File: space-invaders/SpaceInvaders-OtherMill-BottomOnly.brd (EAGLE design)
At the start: 127 x 101.6 mm, 26 parts, among them J2_J4 TM4C123GXL, J3_J1 TM4C123GXL, J5 Nokia 5110, J6 Nokia 5110, U1 5V Voltage Regulator

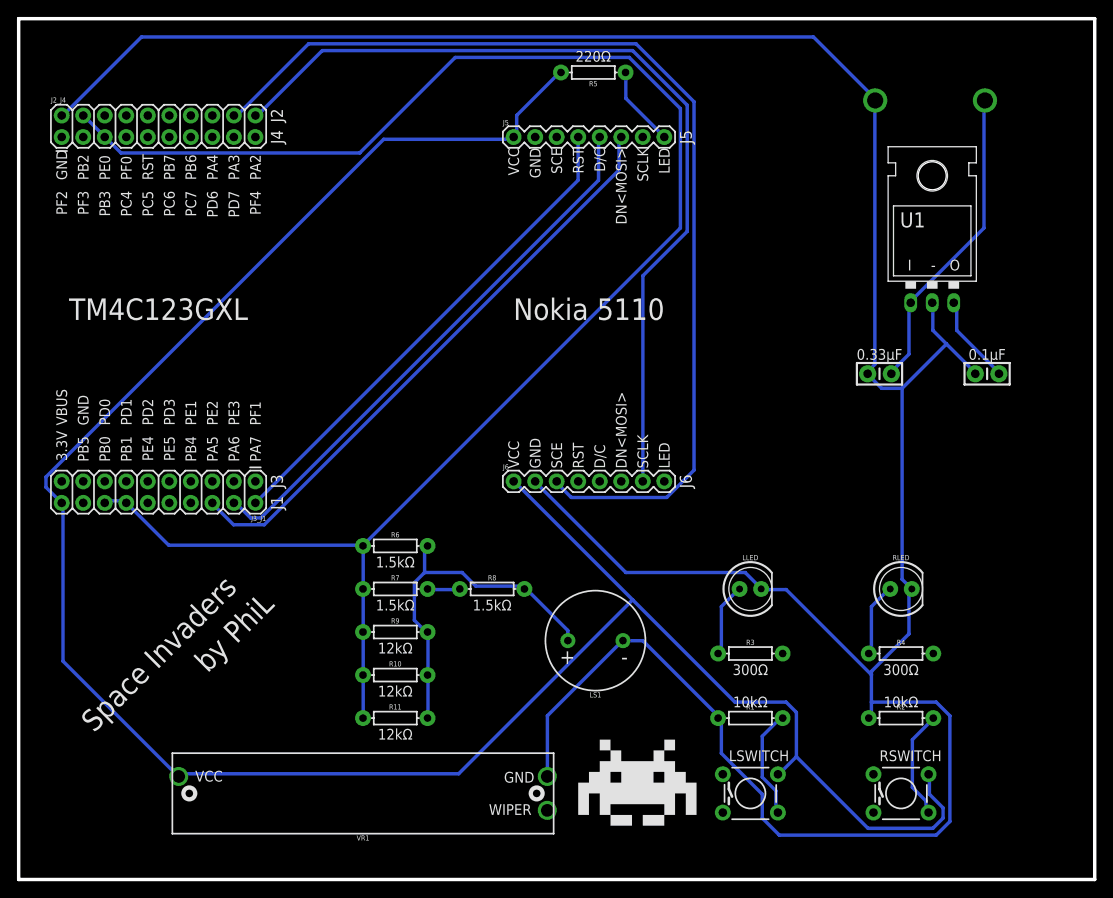
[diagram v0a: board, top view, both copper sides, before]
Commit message: Remove Top layer & Edit Bottom layer
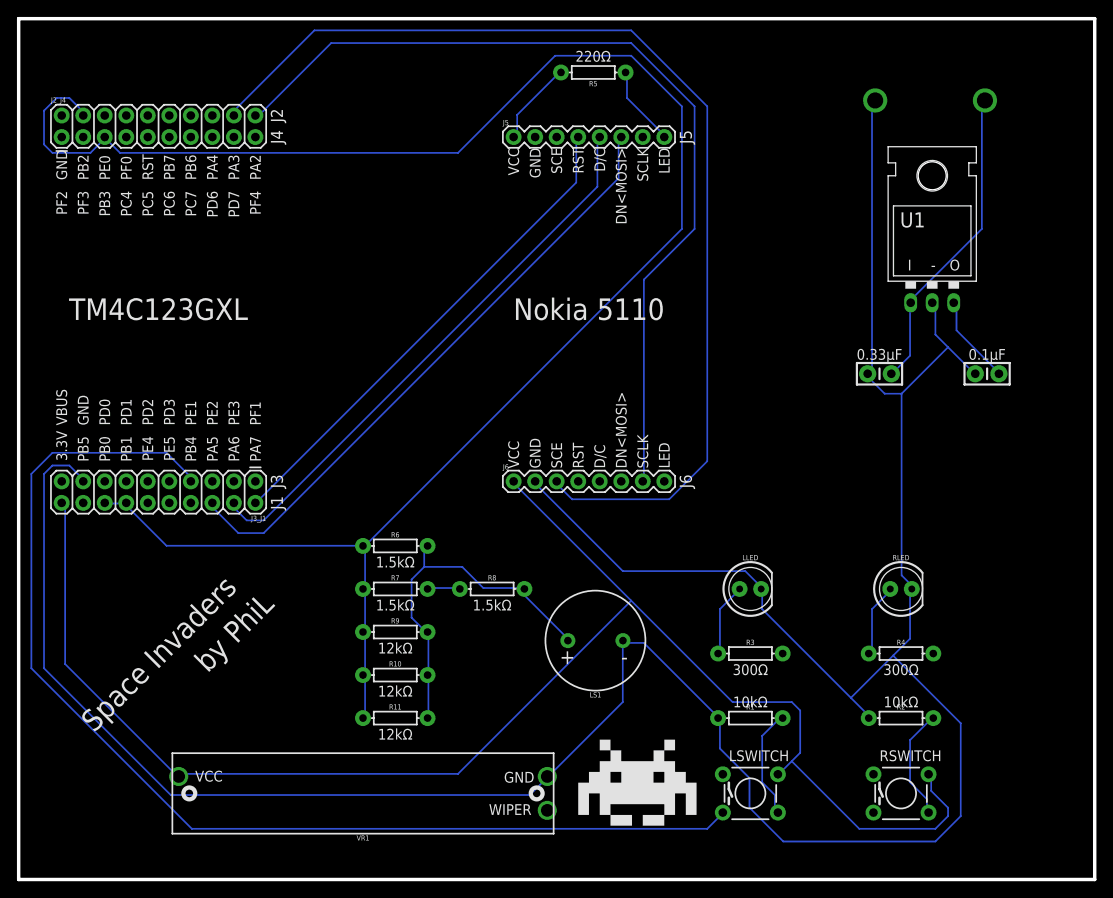
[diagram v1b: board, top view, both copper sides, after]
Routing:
- net PE1: track 0.00 -> 134.8 mm
- net 3.3V: track 266.3 -> 192.7 mm
- net PB2: track 199.9 -> 216.5 mm
- net PA3: track 122.5 -> 127.3 mm
- net GND: track 344.2 -> 341.1 mm
- net PA2: track 103.4 -> 105.2 mm
- net PA5: track 70.4 -> 72.0 mm
- net PA6: track 65.4 -> 66.3 mm
- net N$23: track 42.8 -> 43.4 mm
- removed copper zone on layer 1, net GND

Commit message: Reposition SpaceInvaders board layout
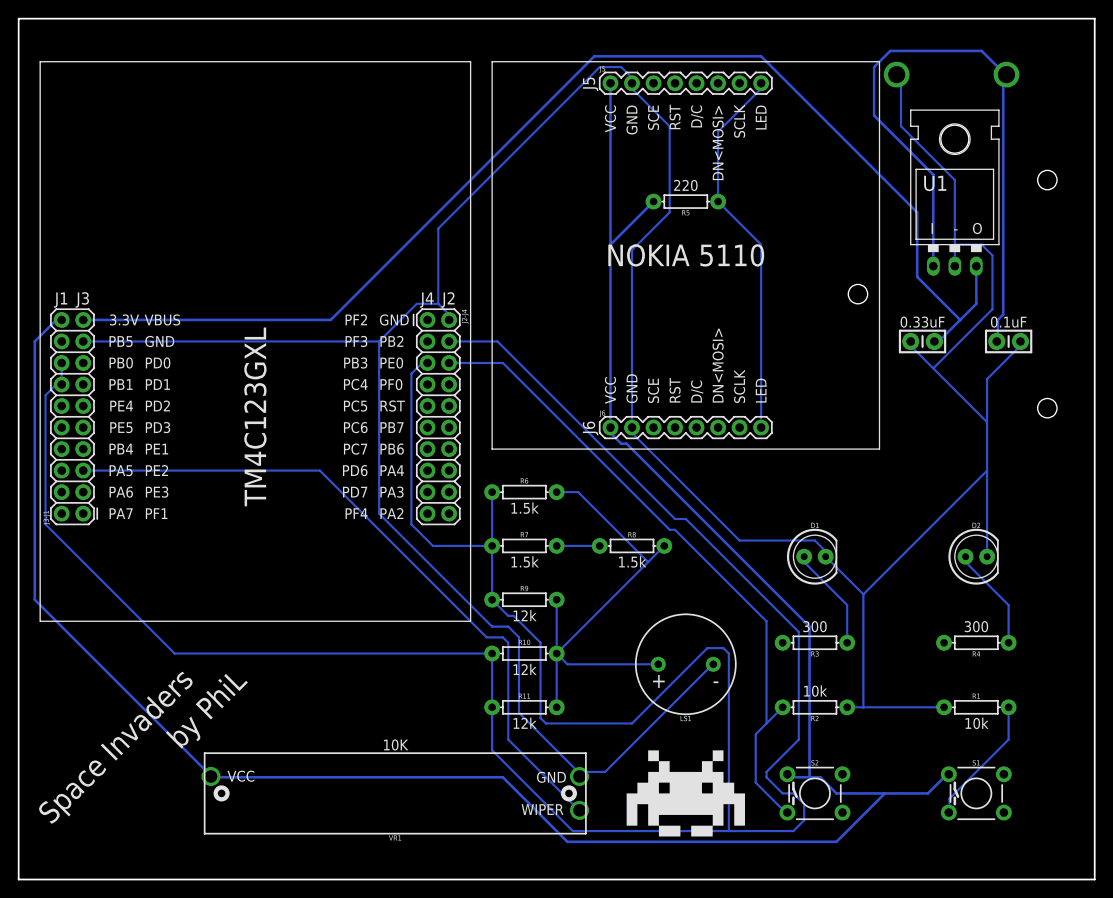
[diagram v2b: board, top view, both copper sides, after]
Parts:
- removed G1: 9V, SparkFun-Batteries:BATTCON_9V
- removed J2_J4, J3_J1: TM4C123GXL, SparkFun-Connectors:2X10
- removed LLED: YELLOW, SparkFun-LED:LED_5MM
- removed LSWITCH, RSWITCH: TACTILE, SparkFun-Retired:TACTILE-PTH
- removed RLED: RED, SparkFun-LED:LED_5MM
- added D1: YELLOW, SparkFun-LED:LED_5MM
- added D2: RED, SparkFun-LED:LED_5MM
- added J2-J4, J3-J1: TM4C123GXL, SparkFun-Connectors:2X10
- added J7: 9V, SparkFun-Connectors:BC9VPC
- added S1: SPECIAL, SparkFun-Switches:TACTILE_SWITCH_PTH_6.0MM
- added S2: REGULAR, SparkFun-Switches:TACTILE_SWITCH_PTH_6.0MM
- C1: value 0.1μF -> 0.1uF
- C2: value 0.33μF -> 0.33uF
- J5, J6: value Nokia 5110 -> Nokia_5110
- LS1: value BUZZER-PTH -> BUZZER
- R1, R2, VR1: value 10kΩ -> 10k
- R10, R11, R9: value 12kΩ -> 12k
- R3, R4: value 300Ω -> 300
- R5: value 220Ω -> 220
- R6, R7, R8: value 1.5kΩ -> 1.5k
- U1: value 5V Voltage Regulator -> LM7805CT
- moved R1 26.7 mm to (113.0, 20.3)
- moved R5 18.7 mm to (78.7, 80.0)
- moved R8 17.3 mm to (72.4, 39.4)
- moved R6 16.5 mm to (59.7, 45.7)
- moved R7 16.1 mm to (59.7, 39.4)
- moved C2 15.7 mm to (116.8, 63.5), turned to 0 degrees
- moved R9 15.7 mm to (59.7, 33.0)
- moved R10 15.5 mm to (59.7, 26.7)
- moved R11 15.3 mm to (59.7, 20.3)
- moved J5 13.1 mm to (69.8, 94.0)
- moved J6 13.1 mm to (69.8, 53.3)
- moved LS1 11.0 mm to (78.7, 25.4)
- moved R2 10.2 mm to (94.0, 20.3), turned to 180 degrees
- moved R4 8.98 mm to (113.0, 27.9), turned to 180 degrees
- moved C1 8.52 mm to (106.7, 63.5)
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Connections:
- net N$23 renamed DAC_OUT
- removed net N$12: LSWITCH.4, R1.P$2
- removed net N$14: R2.P$2, RSWITCH.4
- removed net N$17: R4.P$1, RLED.A
- removed net N$19: LLED.A, R3.P$1
- new net D/C: J6.5
- new net DN<MOSI>: J6.6
- new net LLED: D1.A, R3.P$1
- new net PA4: J2-J4.16
- new net PB6: J2-J4.14
- new net PB7: J2-J4.12
- new net PC4: J2-J4.7
- new net PC5: J2-J4.9
- new net PC6: J2-J4.11
- new net PC7: J2-J4.13
- new net PD0: J3-J1.15
- new net PD1: J3-J1.13
- new net PD2: J3-J1.11
- new net PD3: J3-J1.9
- new net PD6: J2-J4.15
- new net PD7: J2-J4.17
- new net PE3: J3-J1.3
- new net PE4: J3-J1.12
- new net PE5: J3-J1.10
- new net PF0: J2-J4.8
- new net PF1: J3-J1.1
- new net PF2: J2-J4.1
- new net PF3: J2-J4.3
- new net PF4: J2-J4.19
- new net RESET: J2-J4.10
- new net RLED: D2.A, R4.P$1
- new net RST: J6.4
- new net SCE: J5.3
- new net SCLK: J5.7
- net 3.3V: now also J3-J1.20, S1.1, S2.1; no longer J3_J1.20, LSWITCH.2, RSWITCH.2
- net 9V: now also J7.V+; no longer G1.+
- net GND: now also D1.K, D2.K, J2-J4.2, J3-J1.17, J5.2, J7.V-; no longer G1.-, J2_J4.2, J3_J1.17, LLED.K, RLED.K
- net LED: now also J6.8
- net PA2: now also J2-J4.20; no longer J2_J4.20
- net PA3: now also J2-J4.18; no longer J2_J4.18
- net PA5: now also J3-J1.6; no longer J3_J1.6
- net PA6: now also J3-J1.4; no longer J3_J1.4
- net PA7: now also J3-J1.2; no longer J3_J1.2
- net PB2: now also J2-J4.4, J2-J4.5, J3-J1.14, J3-J1.16; no longer J2_J4.4, J2_J4.5, J3_J1.14, J3_J1.16
- net PB4: now also J3-J1.8; no longer J3_J1.8
- net PB5: now also J3-J1.18; no longer J3_J1.18
- net PE0: now also J2-J4.6, R2.P$2, S2.3; no longer J2_J4.6, RSWITCH.3
- net PE1: now also J3-J1.7, R1.P$2, S1.3; no longer J3_J1.7, LSWITCH.3
- net PE2: now also J3-J1.5; no longer J3_J1.5
- net VBUS: now also J3-J1.19; no longer J3_J1.19
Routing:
- net VBUS: track 10.6 -> 145.0 mm
- net PA3: track 127.3 -> 0.00 mm
- net PE1: track 134.8 -> 15.3 mm
- net PA2: track 105.2 -> 0.00 mm
- net PB2: track 216.5 -> 321.4 mm
- net PE2: track 0.00 -> 81.9 mm
- net PE0: track 0.00 -> 77.5 mm
- net 3.3V: track 192.7 -> 269.5 mm
- net PA5: track 72.0 -> 0.00 mm
- net PA6: track 66.3 -> 0.00 mm
- net PA7: track 58.9 -> 0.00 mm
- net GND: track 341.1 -> 384.2 mm
- net 9V: track 36.9 -> 76.0 mm
- net LED: track 9.66 -> 44.8 mm
- net DAC_OUT: track 43.4 -> 57.4 mm
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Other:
- board text added: "0.1uF"
- board text added: "0.33uF"
- board text added: "1.5k"
- board text added: "10K"
- board text added: "10k"
- board text added: "12k"
- board text added: "220"
- board text added: "300"
- board text added: "NOKIA 5110"
- board text removed: "0.1μF"
- board text removed: "0.33μF"
- board text removed: "1.5kΩ"
- board text removed: "10kΩ"
- board text removed: "12kΩ"
- board text removed: "220Ω"
- board text removed: "300Ω"
- board text removed: "Nokia 5110"
